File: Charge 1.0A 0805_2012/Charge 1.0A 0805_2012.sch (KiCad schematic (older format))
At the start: 13 parts, among them U1 MCP73833T

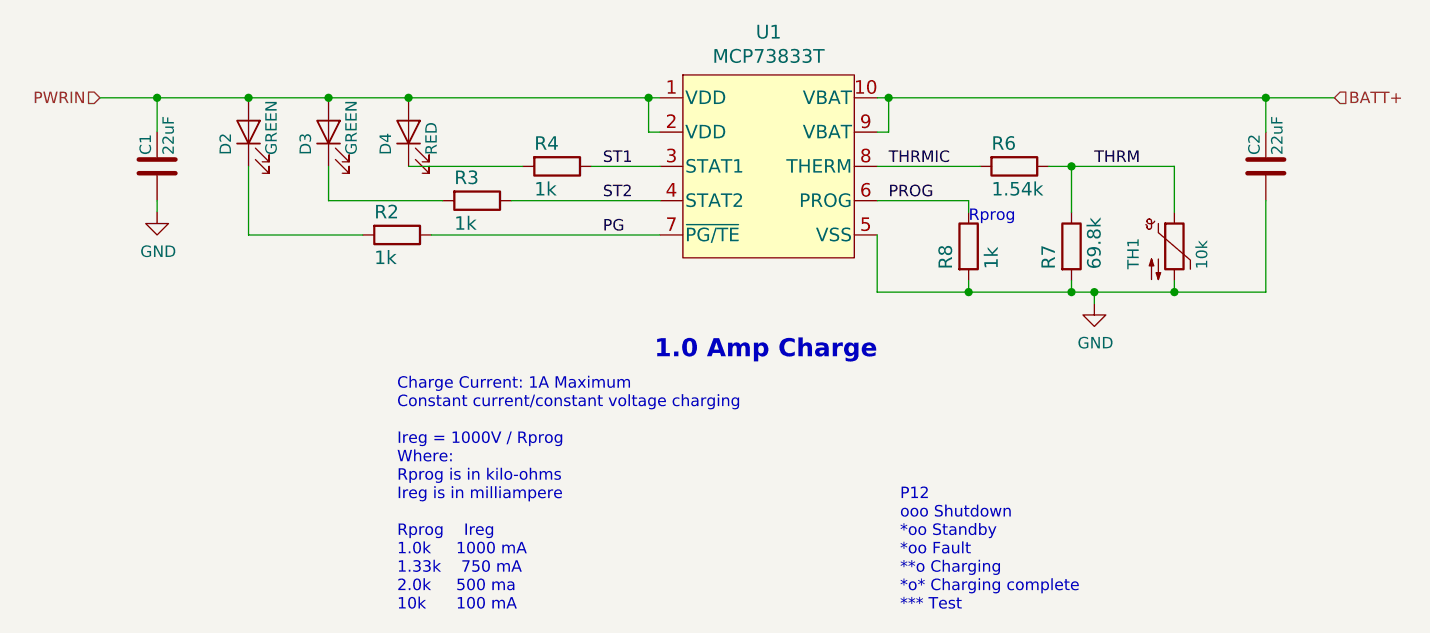
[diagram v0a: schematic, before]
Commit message: Updated Li-Ion schematics
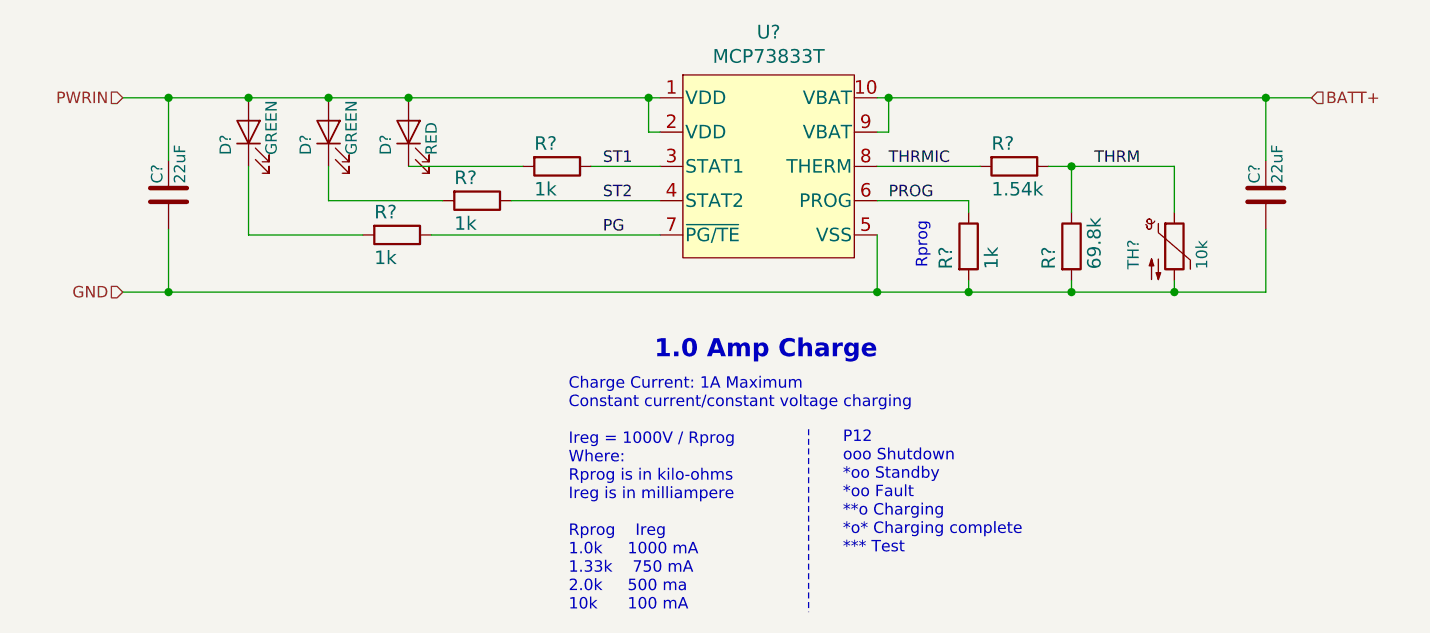
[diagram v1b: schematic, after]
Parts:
- renumbered C2 to C?, C1 to C?, D2 to D?, D3 to D?, D4 to D?, R8 to R?, R6 to R?, R7 to R?, R4 to R?, R3 to R?, R2 to R?, TH1 to TH?, U1 to U?
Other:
- moved on the sheet: C?
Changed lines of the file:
@@
 1.0 Amp Charge
 $Comp
-L Li_Ion_LE:MCP73833T U1
+L Li_Ion_LE:MCP73833T U?
 U 1 1 5EB6C38E
 P 5600 3450
-F 0 "U1" H 5575 3937 60  0000 C CNN
+F 0 "U?" H 5575 3937 60  0000 C CNN
 F 1 "MCP73833T" H 5575 3831 60  0000 C CNN
 F 2 "Li_Ion_LE:MCP73833" H 5600 2850 60  0001 C CNN
@@
 PROG
 $Comp
-L Frequently_Used_LE:LED D3
+L Frequently_Used_LE:LED D?
 U 1 1 5EBA8419
 P 3650 3400
-F 0 "D3" H 3550 3500 50  0000 L CNN
+F 0 "D?" H 3550 3500 50  0000 L CNN
 F 1 "GREEN" H 3550 3300 50  0000 L CNN
 F 2 "Frequently_Used_LE:LED_0805_2012Metric" H 3650 3400 50  0001 C CNN
@@
 $EndComp
 $Comp
-L Frequently_Used_LE:LED D4
+L Frequently_Used_LE:LED D?
 U 1 1 5EBA883B
 P 4000 3400
-F 0 "D4" H 3900 3500 50  0000 L CNN
+F 0 "D?" H 3900 3500 50  0000 L CNN
 F 1 "RED" H 3900 3300 50  0000 L CNN
 F 2 "Frequently_Used_LE:LED_0805_2012Metric" H 4000 3400 50  0001 C CNN
@@
 $EndComp
 $Comp
-L Frequently_Used_LE:R R4
+L Frequently_Used_LE:R R?
 U 1 1 5EBD0C80
 P 4650 3550
-F 0 "R4" V 4550 3450 59  0000 L CNN
+F 0 "R?" V 4550 3450 59  0000 L CNN
 F 1 "1k" V 4750 3450 59  0000 L CNN
 F 2 "Frequently_Used_LE:0805_2012Metric" H 4650 3550 50  0001 C CNN
@@
 	3300 3850 3300 3550
 $Comp
-L Frequently_Used_LE:R R3
+L Frequently_Used_LE:R R?
 U 1 1 5EBEA227
 P 4300 3700
-F 0 "R3" V 4200 3600 59  0000 L CNN
+F 0 "R?" V 4200 3600 59  0000 L CNN
 F 1 "1k" V 4400 3600 59  0000 L CNN
 F 2 "Frequently_Used_LE:0805_2012Metric" H 4300 3700 50  0001 C CNN
@@
 $EndComp
 $Comp
-L Frequently_Used_LE:R R2
+L Frequently_Used_LE:R R?
 U 1 1 5EBF1B19
 P 3950 3850
-F 0 "R2" V 3850 3750 59  0000 L CNN
+F 0 "R?" V 3850 3750 59  0000 L CNN
 F 1 "1k" V 4050 3750 59  0000 L CNN
 F 2 "Frequently_Used_LE:0805_2012Metric" H 3950 3850 50  0001 C CNN
@@
 Connection ~ 6900 4100
 Wire Wire Line
-	6900 4100 7000 4100
-Wire Wire Line
 	7350 4050 7350 4100
 Connection ~ 7350 4100
@@
 	6050 3250 6100 3250
 $Comp
-L Frequently_Used_LE:R R6
+L Frequently_Used_LE:R R?
 U 1 1 5EB9EAAB
 P 6650 3550
-F 0 "R6" V 6550 3450 59  0000 L CNN
+F 0 "R?" V 6550 3450 59  0000 L CNN
 F 1 "1.54k" V 6750 3450 59  0000 L CNN
 F 2 "Frequently_Used_LE:0805_2012Metric" H 6650 3550 50  0001 C CNN
@@
 Wire Wire Line
 	3650 3700 4150 3700
-$Comp
-L Frequently_Used_LE:C C2
-U 1 1 5EB4A5BF
-P 7750 3550
-F 0 "C2" V 7700 3600 50  0000 L CNN
-F 1 "22uF" V 7800 3600 50  0000 L CNN
-F 2 "Frequently_Used_LE:0805_2012Metric" H 7788 3400 50  0001 C CNN
-F 3 "https://media.digikey.com/pdf/Data%20Sheets/Samsung%20PDFs/CL_Series_MLCC_ds.pdf" H 7750 3550 50  0001 C CNN
-F 4 "22µF ±10% 6.3V Ceramic Capacitor X5R 0805 (2012 Metric)" H 7750 3550 50  0001 C CNN "Description"
-F 5 "Digikey" H 7750 3550 50  0001 C CNN "Source"
-F 6 "1276-6687-1-ND" H 7750 3550 50  0001 C CNN "Source Part No."
-F 7 "Samsung Electro-Mechanics" H 7750 3550 50  0001 C CNN "Manufacturer Name"
-F 8 "CL21A226KQCLRNC" H 7750 3550 50  0001 C CNN "Manufacturer Part No."
-	1    7750 3550
-	1    0    0    -1
-$EndComp
-$Comp
-L Frequently_Used_LE:C C1
-U 1 1 5EB4C1AB
-P 2900 3550
-F 0 "C1" V 2850 3600 50  0000 L CNN
-F 1 "22uF" V 2950 3600 50  0000 L CNN
-F 2 "Frequently_Used_LE:0805_2012Metric" H 2938 3400 50  0001 C CNN
-F 3 "https://media.digikey.com/pdf/Data%20Sheets/Samsung%20PDFs/CL_Series_MLCC_ds.pdf" H 2900 3550 50  0001 C CNN
-F 4 "22µF ±10% 6.3V Ceramic Capacitor X5R 0805 (2012 Metric)" H 2900 3550 50  0001 C CNN "Description"
-F 5 "Digikey" H 2900 3550 50  0001 C CNN "Source"
-F 6 "1276-6687-1-ND" H 2900 3550 50  0001 C CNN "Source Part No."
-F 7 "Samsung Electro-Mechanics" H 2900 3550 50  0001 C CNN "Manufacturer Name"
-F 8 "CL21A226KQCLRNC" H 2900 3550 50  0001 C CNN "Manufacturer Part No."
-	1    2900 3550
-	1    0    0    -1
-$EndComp
-Wire Wire Line
-	7750 3700 7750 4100
 Wire Wire Line
 	7350 4100 7750 4100
-Wire Wire Line
-	7750 3400 7750 3250
-Wire Wire Line
-	2900 3250 2900 3400
-$Comp
-L Frequently_Used_LE:GND #PWR02
-U 1 1 5EB673E3
-P 7000 4150
-F 0 "#PWR02" H 7000 3900 50  0001 C CNN
-F 1 "GND" H 7005 3977 50  0000 C CNN
-F 2 "" H 7000 4150 50  0001 C CNN
-F 3 "" H 7000 4150 50  0001 C CNN
-	1    7000 4150
-	1    0    0    -1
-$EndComp
-Wire Wire Line
-	7000 4150 7000 4100
-Connection ~ 7000 4100
-Wire Wire Line
-	7000 4100 7350 4100
-$Comp
-L Frequently_Used_LE:GND #PWR01
-U 1 1 5EB6C4AE
-P 2900 3750
-F 0 "#PWR01" H 2900 3500 50  0001 C CNN
-F 1 "GND" H 2905 3577 50  0000 C CNN
-F 2 "" H 2900 3750 50  0001 C CNN
-F 3 "" H 2900 3750 50  0001 C CNN
-	1    2900 3750
-	1    0    0    -1
-$EndComp
-Wire Wire Line
-	2900 3700 2900 3750
 Text Label 6100 3550 0    50   ~ 0
 THRMIC
@@
 Wire Wire Line
 	4800 3550 5100 3550
-Connection ~ 2900 3250
-Wire Wire Line
-	2650 3250 2900 3250
+Connection ~ 2950 3250
+Wire Wire Line
+	2750 3250 2950 3250
 Connection ~ 7750 3250
 Wire Wire Line
-	7750 3250 8050 3250
-$Comp
-L Li_Ion_LE:Thermistor_NTC TH1
+	7750 3250 7950 3250
+$Comp
+L Li_Ion_LE:Thermistor_NTC TH?
 U 1 1 5EBC49A8
 P 7350 3900
-F 0 "TH1" V 7200 3800 50  0000 L BNN
+F 0 "TH?" V 7200 3800 50  0000 L BNN
 F 1 "10k" V 7500 3800 50  0000 L BNN
 F 2 "Frequently_Used_LE:0805_2012Metric" H 7350 3950 50  0001 C CNN
@@
 $EndComp
 $Comp
-L Frequently_Used_LE:R R8
+L Frequently_Used_LE:R R?
 U 1 1 5EB60D47
 P 6450 3900
-F 0 "R8" V 6350 3800 59  0000 L CNN
+F 0 "R?" V 6350 3800 59  0000 L CNN
 F 1 "1k" V 6550 3800 59  0000 L CNN
 F 2 "Frequently_Used_LE:0805_2012Metric" H 6450 3900 50  0001 C CNN
@@
 $EndComp
 $Comp
-L Frequently_Used_LE:R R7
+L Frequently_Used_LE:R R?
 U 1 1 5EBB9C41
 P 6900 3900
-F 0 "R7" V 6800 3800 59  0000 L CNN
+F 0 "R?" V 6800 3800 59  0000 L CNN
 F 1 "69.8k" V 7000 3800 59  0000 L CNN
 F 2 "Frequently_Used_LE:0805_2012Metric" H 6900 3900 50  0001 C CNN
@@
 	6100 3250 7750 3250
 $Comp
-L Frequently_Used_LE:LED D2
+L Frequently_Used_LE:LED D?
 U 1 1 5EBA65E2
 P 3300 3400
-F 0 "D2" H 3200 3500 50  0000 L CNN
+F 0 "D?" H 3200 3500 50  0000 L CNN
 F 1 "GREEN" H 3200 3300 50  0000 L CNN
 F 2 "Frequently_Used_LE:LED_0805_2012Metric" H 3300 3400 50  0001 C CNN
@@
 $EndComp
 Wire Wire Line
-	2900 3250 3300 3250
+	2950 3250 3300 3250
 Connection ~ 3300 3250
 Wire Wire Line
@@
 Wire Wire Line
 	4000 3250 5050 3250
-Text HLabel 2650 3250 0    50   Input ~ 0
+Text HLabel 2750 3250 0    50   Input ~ 0
 PWRIN
-Text HLabel 8050 3250 2    50   Input ~ 0
+Text HLabel 7950 3250 2    50   Input ~ 0
 BATT+
-Text Notes 3950 5500 0    50   ~ 0
+Text Notes 6275 4000 1    50   ~ 0
+Rprog
+Text Notes 5900 5250 0    50   ~ 0
+P12\nooo Shutdown\n*oo Standby\n*oo Fault\n**o Charging\n*o* Charging complete\n*** Test\n
+Wire Notes Line style solid
+	5750 4700 5750 5500
+Text Notes 4700 5500 0    50   ~ 0
 Charge Current: 1A Maximum\nConstant current/constant voltage charging\n\nIreg = 1000V / Rprog\nWhere:\nRprog is in kilo-ohms\nIreg is in milliampere\n\nRprog    Ireg\n1.0k     1000 mA\n1.33k    750 mA\n2.0k     500 ma\n10k      100 mA
-Text Notes 6450 3800 0    50   ~ 0
-Rprog
-Text Notes 6150 5500 0    50   ~ 0
-P12\nooo Shutdown\n*oo Standby\n*oo Fault\n**o Charging\n*o* Charging complete\n*** Test\n
+Wire Wire Line
+	6900 4100 7350 4100
+Wire Wire Line
+	6050 4100 2950 4100
+Connection ~ 6050 4100
+Connection ~ 2950 4100
+$Comp
+L Frequently_Used_LE:C C?
+U 1 1 5EB4C1AB
+P 2950 3675
+F 0 "C?" V 2900 3725 50  0000 L CNN
+F 1 "22uF" V 3000 3725 50  0000 L CNN
+F 2 "Frequently_Used_LE:0805_2012Metric" H 2988 3525 50  0001 C CNN
+F 3 "https://media.digikey.com/pdf/Data%20Sheets/Samsung%20PDFs/CL_Series_MLCC_ds.pdf" H 2950 3675 50  0001 C CNN
+F 4 "22µF ±10% 6.3V Ceramic Capacitor X5R 0805 (2012 Metric)" H 2950 3675 50  0001 C CNN "Description"
+F 5 "Digikey" H 2950 3675 50  0001 C CNN "Source"
+F 6 "1276-6687-1-ND" H 2950 3675 50  0001 C CNN "Source Part No."
+F 7 "Samsung Electro-Mechanics" H 2950 3675 50  0001 C CNN "Manufacturer Name"
+F 8 "CL21A226KQCLRNC" H 2950 3675 50  0001 C CNN "Manufacturer Part No."
+	1    2950 3675
+	1    0    0    -1
+$EndComp
+Wire Wire Line
+	2950 3250 2950 3525
+Wire Wire Line
+	2950 3825 2950 4100
+Wire Wire Line
+	2950 4100 2750 4100
+Text HLabel 2750 4100 0    50   Input ~ 0
+GND
+Wire Wire Line
+	7750 3825 7750 4100
+Wire Wire Line
+	7750 3525 7750 3250
+$Comp
+L Frequently_Used_LE:C C?
+U 1 1 5EB4A5BF
+P 7750 3675
+F 0 "C?" V 7700 3725 50  0000 L CNN
+F 1 "22uF" V 7800 3725 50  0000 L CNN
+F 2 "Frequently_Used_LE:0805_2012Metric" H 7788 3525 50  0001 C CNN
+F 3 "https://media.digikey.com/pdf/Data%20Sheets/Samsung%20PDFs/CL_Series_MLCC_ds.pdf" H 7750 3675 50  0001 C CNN
+F 4 "22µF ±10% 6.3V Ceramic Capacitor X5R 0805 (2012 Metric)" H 7750 3675 50  0001 C CNN "Description"
+F 5 "Digikey" H 7750 3675 50  0001 C CNN "Source"
+F 6 "1276-6687-1-ND" H 7750 3675 50  0001 C CNN "Source Part No."
+F 7 "Samsung Electro-Mechanics" H 7750 3675 50  0001 C CNN "Manufacturer Name"
+F 8 "CL21A226KQCLRNC" H 7750 3675 50  0001 C CNN "Manufacturer Part No."
+	1    7750 3675
+	1    0    0    -1
+$EndComp
 $EndSCHEMATC
